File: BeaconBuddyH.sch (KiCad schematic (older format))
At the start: 24 parts, among them P1 CONN_01X06, U1 nRF52832-QFAA, Y1 32.768kHz, Y2 32MHz

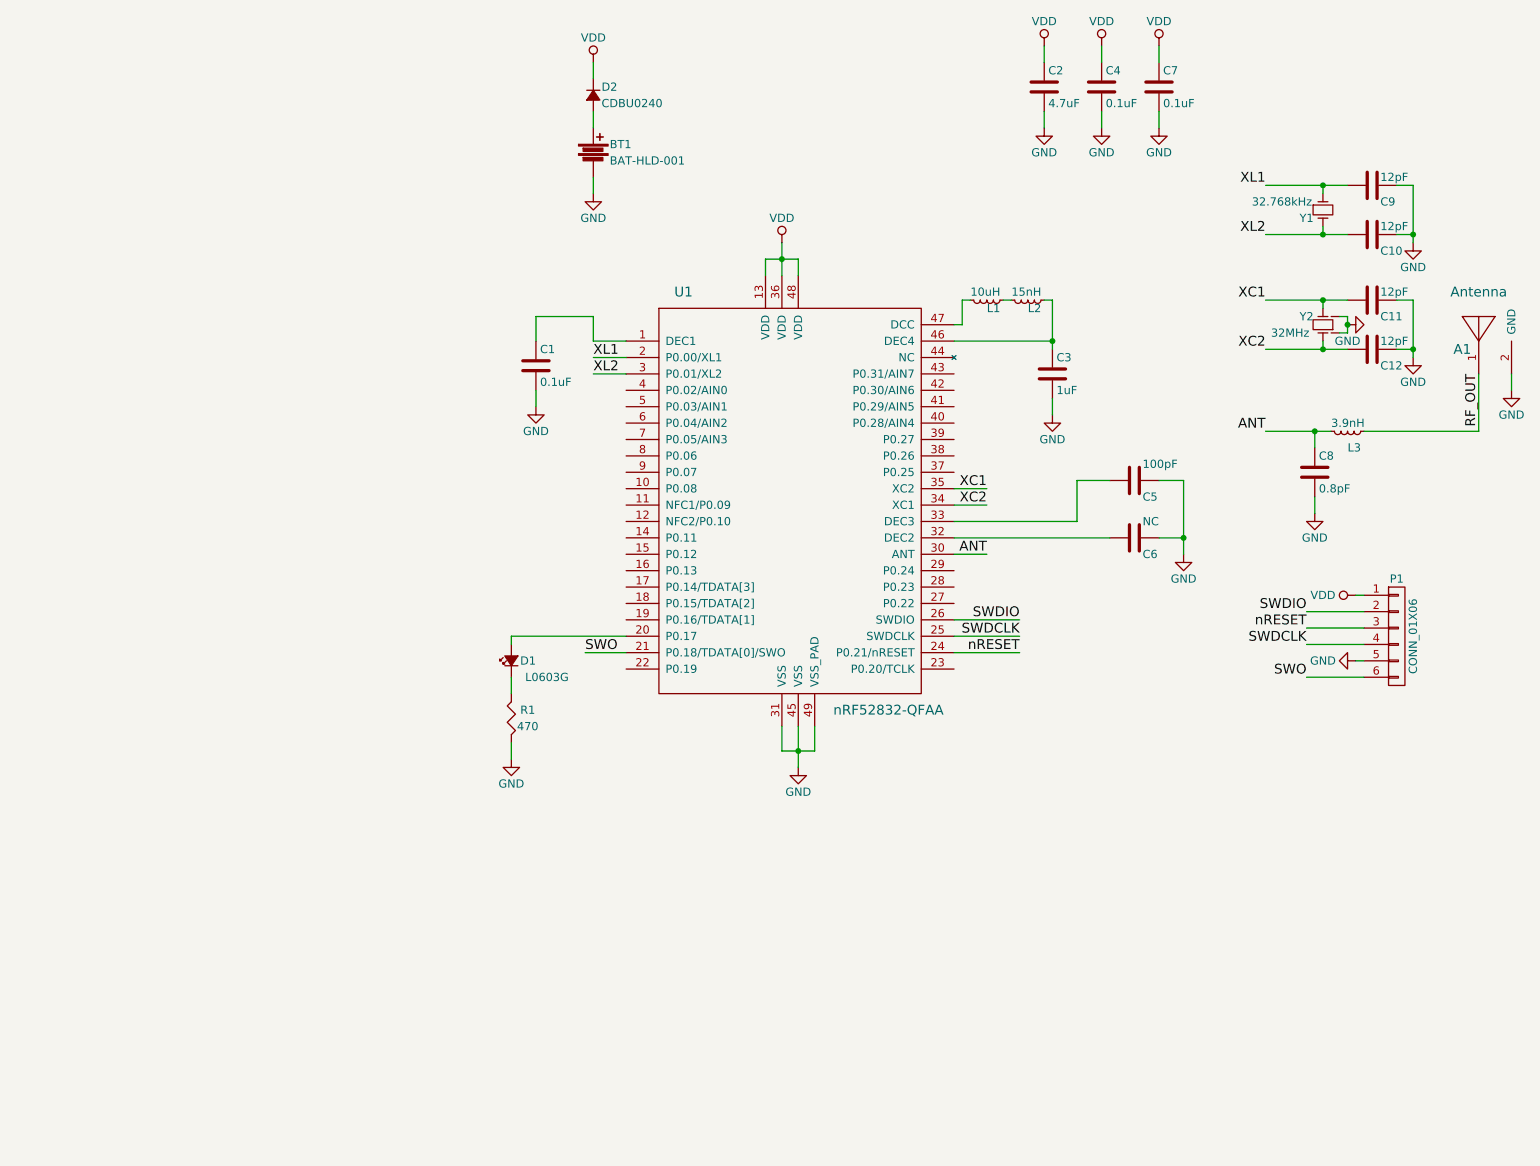
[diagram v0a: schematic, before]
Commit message: Added Temp/Humidity sensor
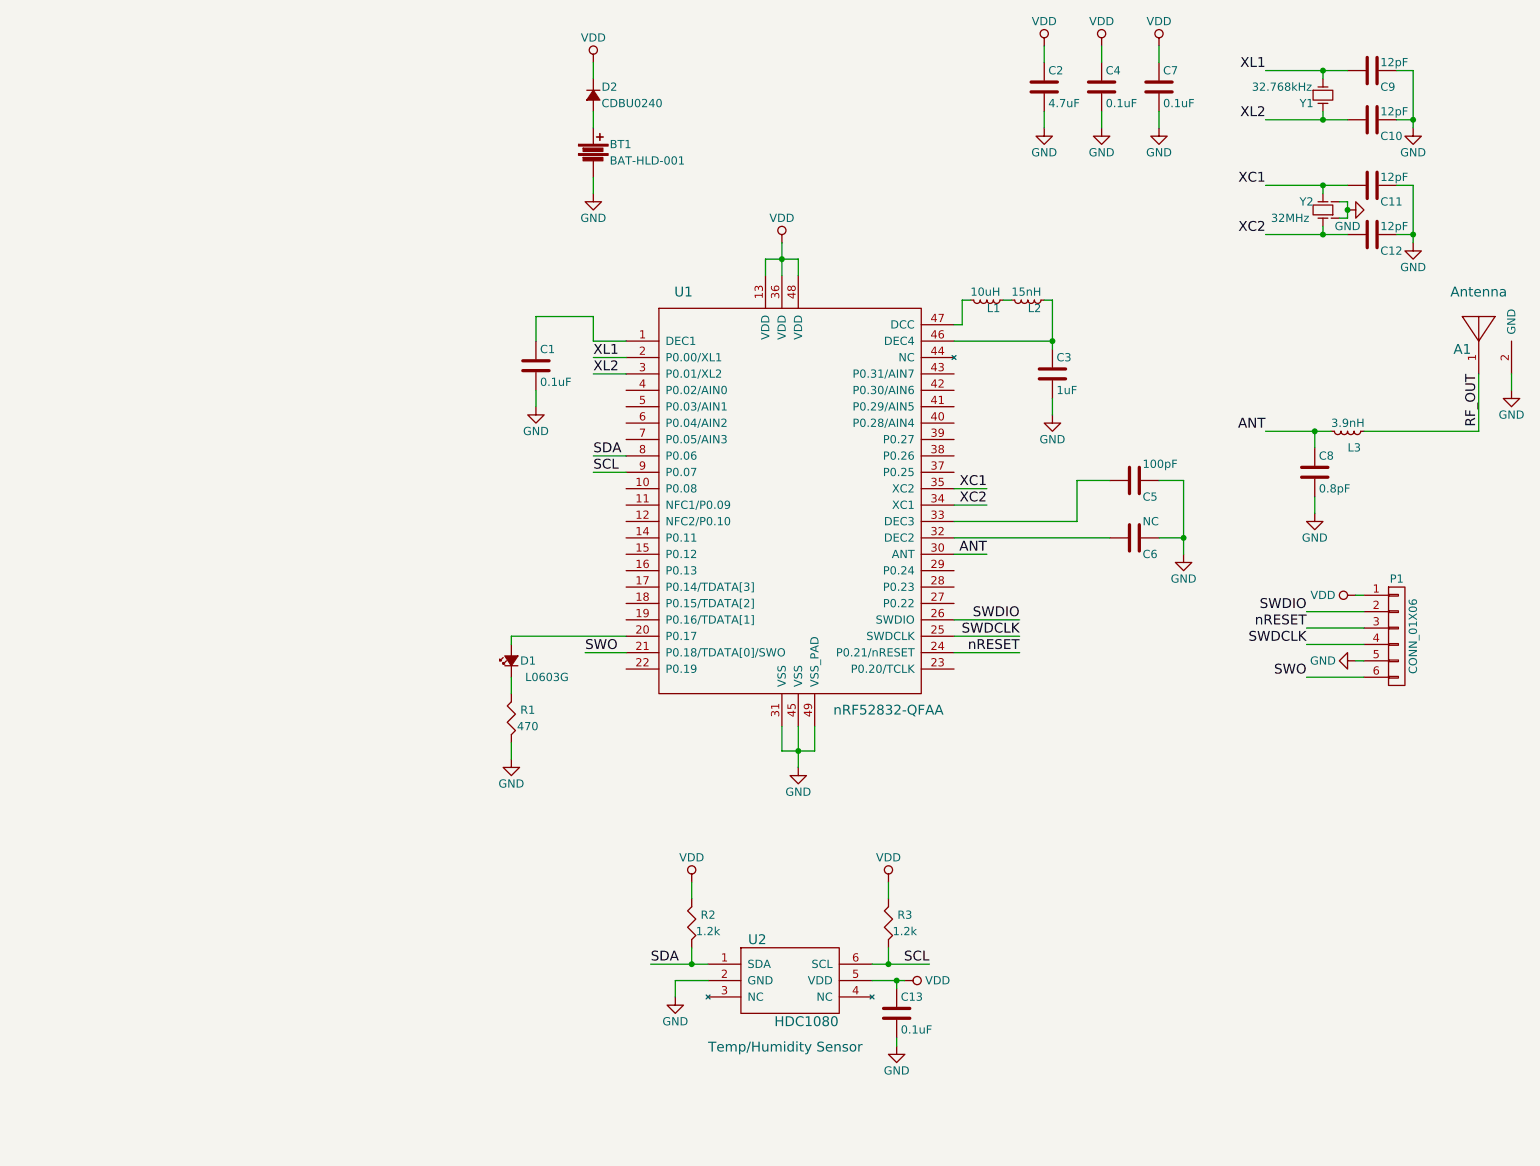
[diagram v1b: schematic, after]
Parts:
- added C13: 0.1uF, Capacitors_SMD:C_0603, symbol C
- added R2, R3: 1.2k, Resistors_SMD:R_0603, symbol R
- added U2: HDC1080, New_Footprints:S-PWSON-N6, symbol HDC1080
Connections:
- net GND: now also C13.2, U2.2 (GND)
- net VDD: now also C13.1, R2.1, R3.1, U2.5 (VDD)
- net SDA: now reaches U1.8 (P0.06)
- net SDA: now also R2.2, U2.1 (SDA)
- net SCL: now reaches U1.9 (P0.07)
- net SCL: now also R3.2, U2.6 (SCL)
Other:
- note added: "Temp/Humidity Sensor"
- moved on the sheet: C10, C11, C12, C9, Y1, Y2

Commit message: Added Pressure Sensor
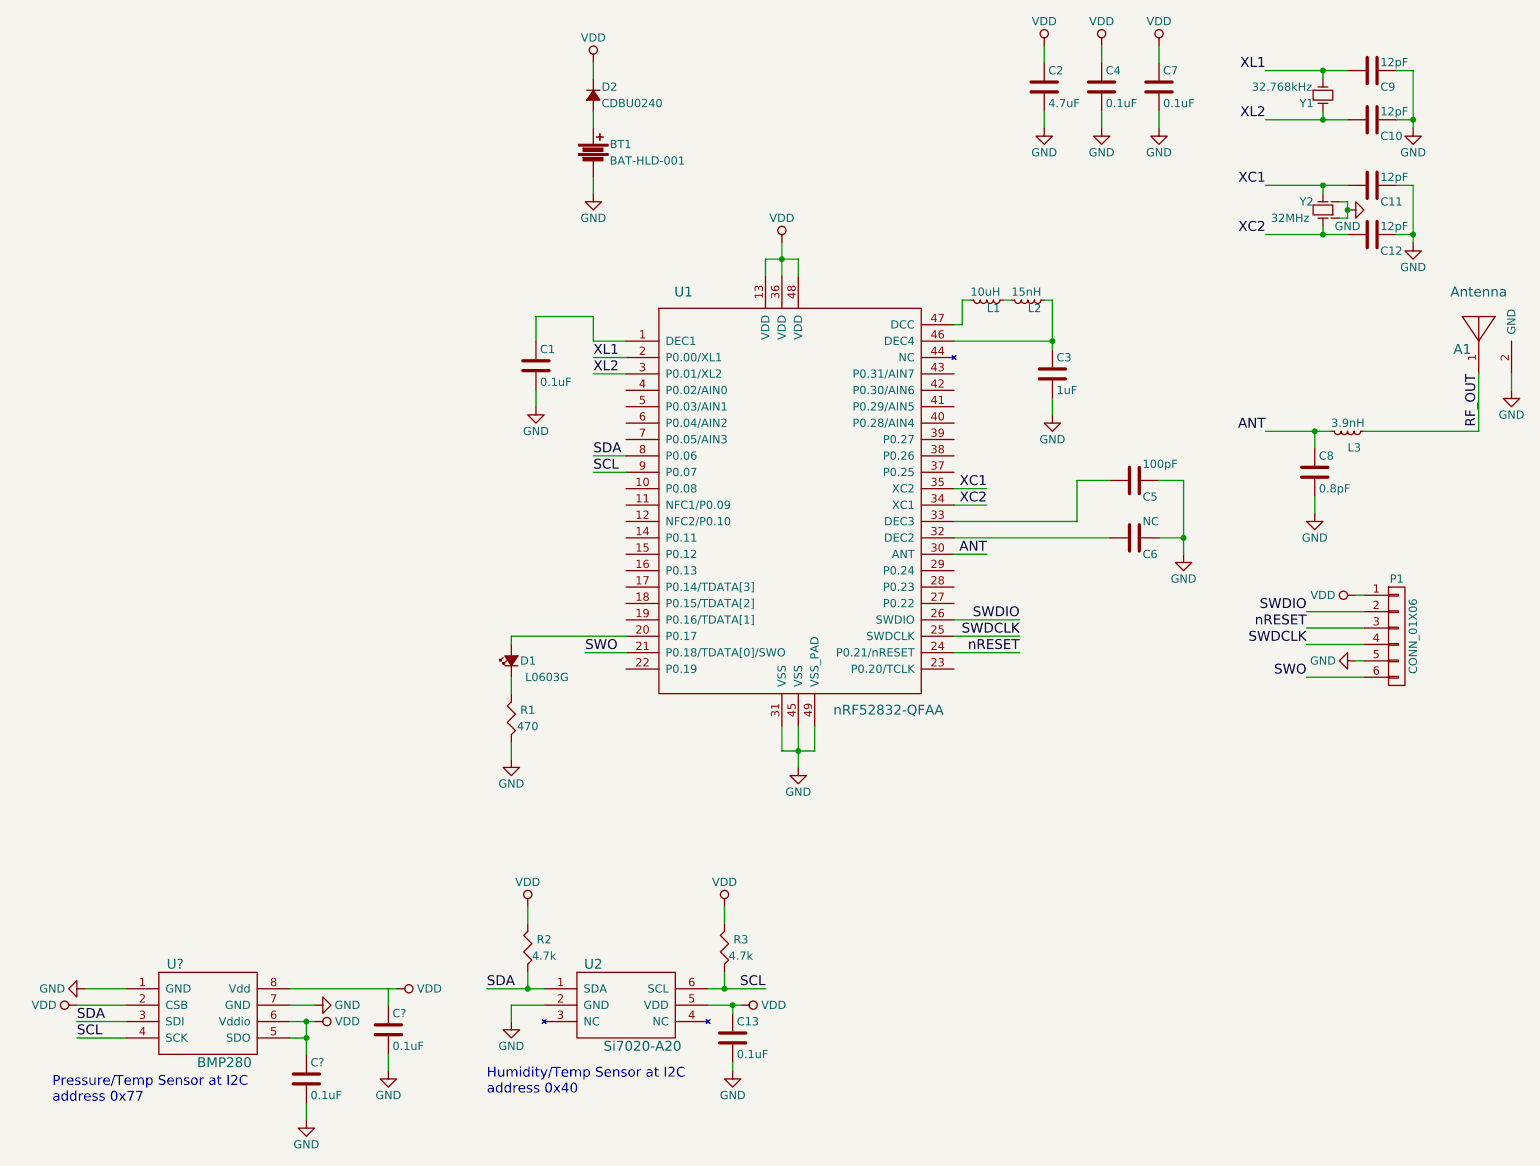
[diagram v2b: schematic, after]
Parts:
- added C? (x2): 0.1uF, Capacitors_SMD:C_0603, symbol C
- added U?: BMP280, symbol BMP280
- R2, R3: value 1.2k -> 4.7k
- U2: value HDC1080 -> Si7020-A20
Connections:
- net GND: now also C?.2, C?.2, U?.1 (GND), U?.7 (GND)
- net SCL: now also U?.4 (SCK)
- net SDA: now also U?.3 (SDI)
- net VDD: now also C?.1, U?.2 (CSB), U?.5 (SDO), U?.6 (Vddio), U?.8 (Vdd)
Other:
- note added: "Humidity/Temp Sensor at I2C\naddress 0x40"
- note added: "Pressure/Temp Sensor at I2C\naddress 0x77"
- note removed: "Temp/Humidity Sensor"
- moved on the sheet: C13, R2, R3, U2

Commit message: Added optional Anemometer/Analog Input
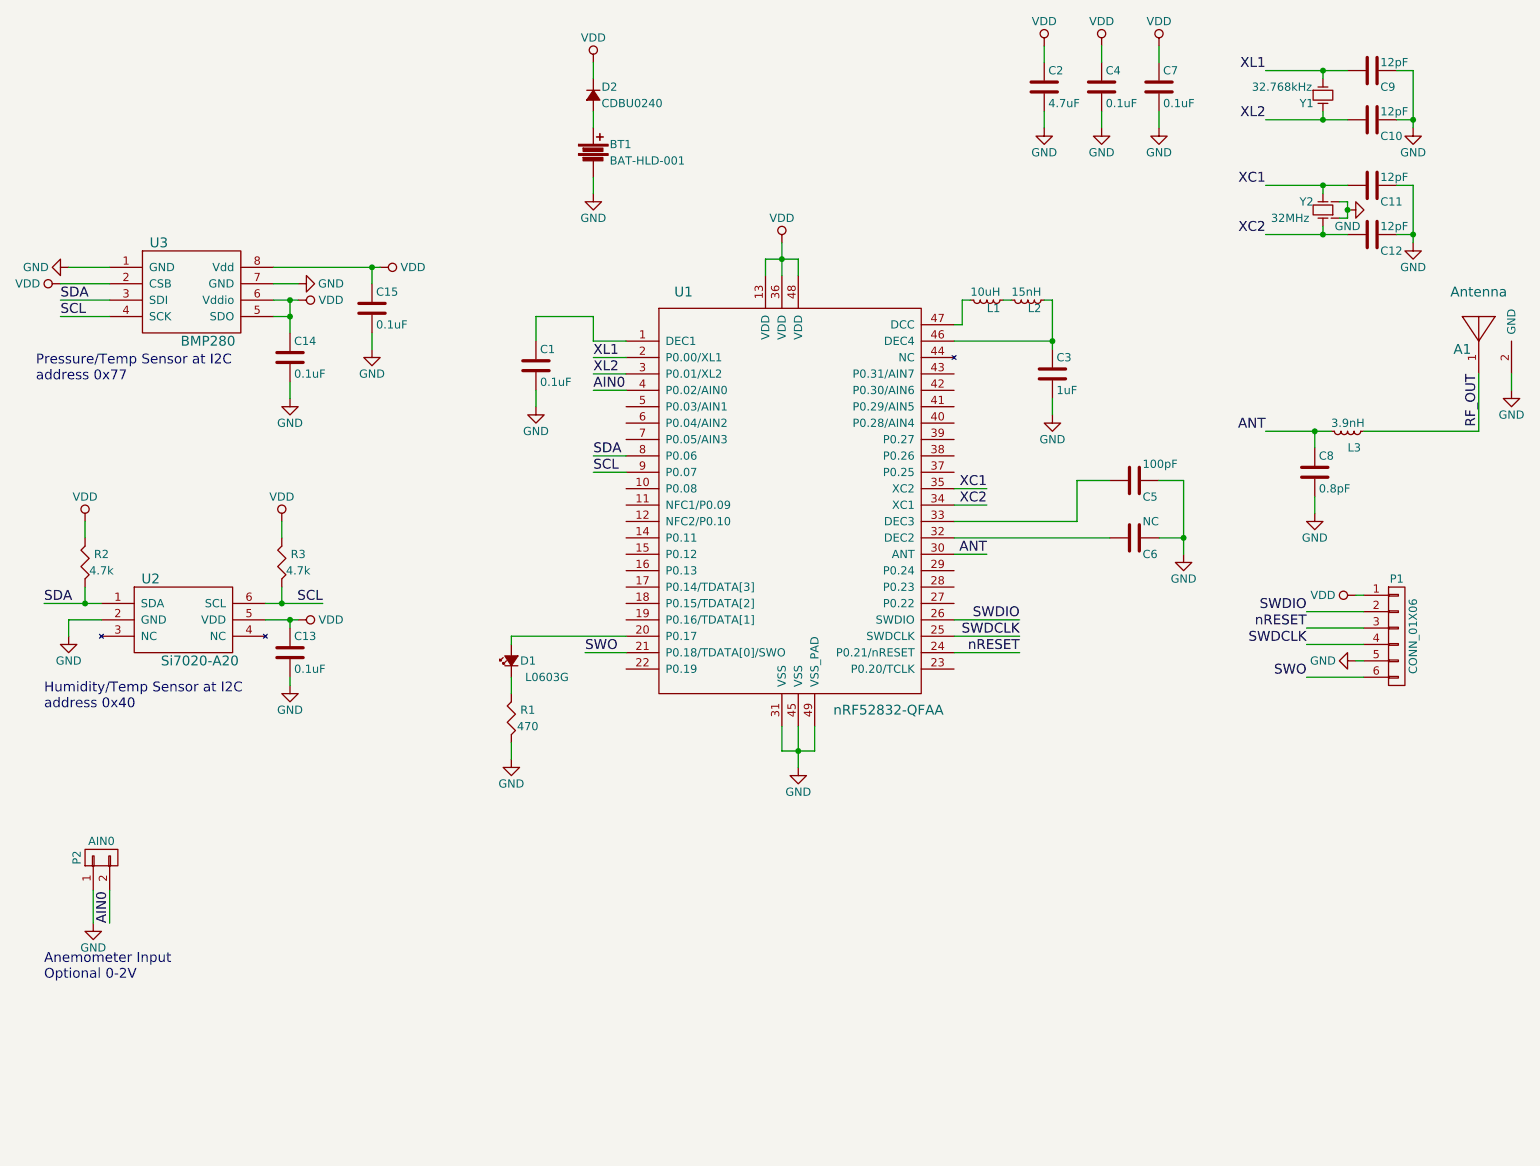
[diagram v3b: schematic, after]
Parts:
- added P2: AIN0, New_Footprints:CONN_100mil_1x2, symbol CONN_01X02
- U3: renamed from U?; footprint (none) -> New_Footprints:Bosch_LGA8
- gave numbers to parts that had none: 2
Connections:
- net GND: now also P2.1 (P1)
- net VDD: now also C15.1
- net AIN0: now reaches U1.4 (P0.02/AIN0)
- net AIN0: now also P2.2 (P2)
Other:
- note added: "Anemometer Input\nOptional 0-2V"
- moved on the sheet: C13, C14, C15, R2, R3, U2, U3
